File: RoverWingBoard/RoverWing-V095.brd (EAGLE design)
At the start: 81.3 x 81.3 mm, 80 parts, among them J1 HEADER-VH, J10 HEADER-PH-4P, J11 HEADER-PH-3P, J12 HEADER-3X04, J13 HEADER-3X06", J14 HEADER-2X16, J15 HEADER-2X12, J16 DF13-4P-1.25DSA, J17 DF13-6P-1.25DSA, J2 HEADER-VH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

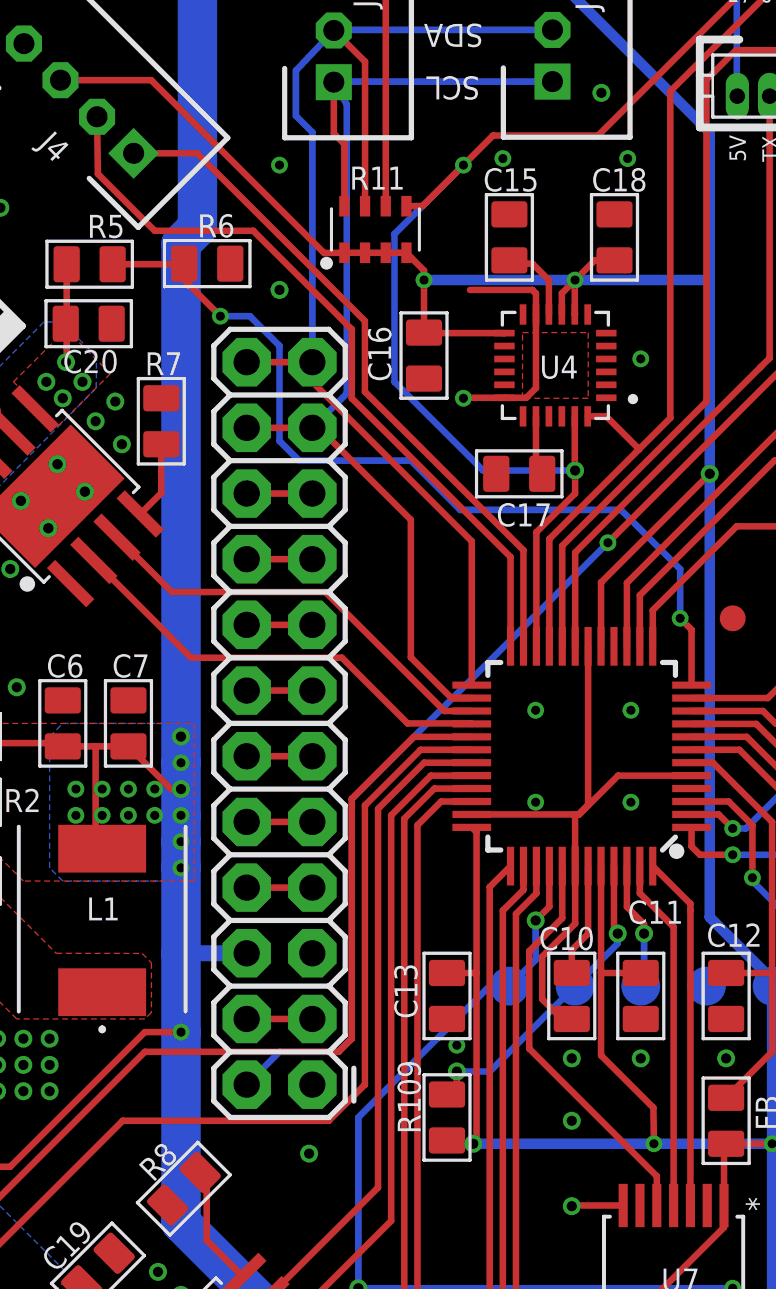
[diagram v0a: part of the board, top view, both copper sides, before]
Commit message: V095 - fixed NeoPixel signals and added the covers
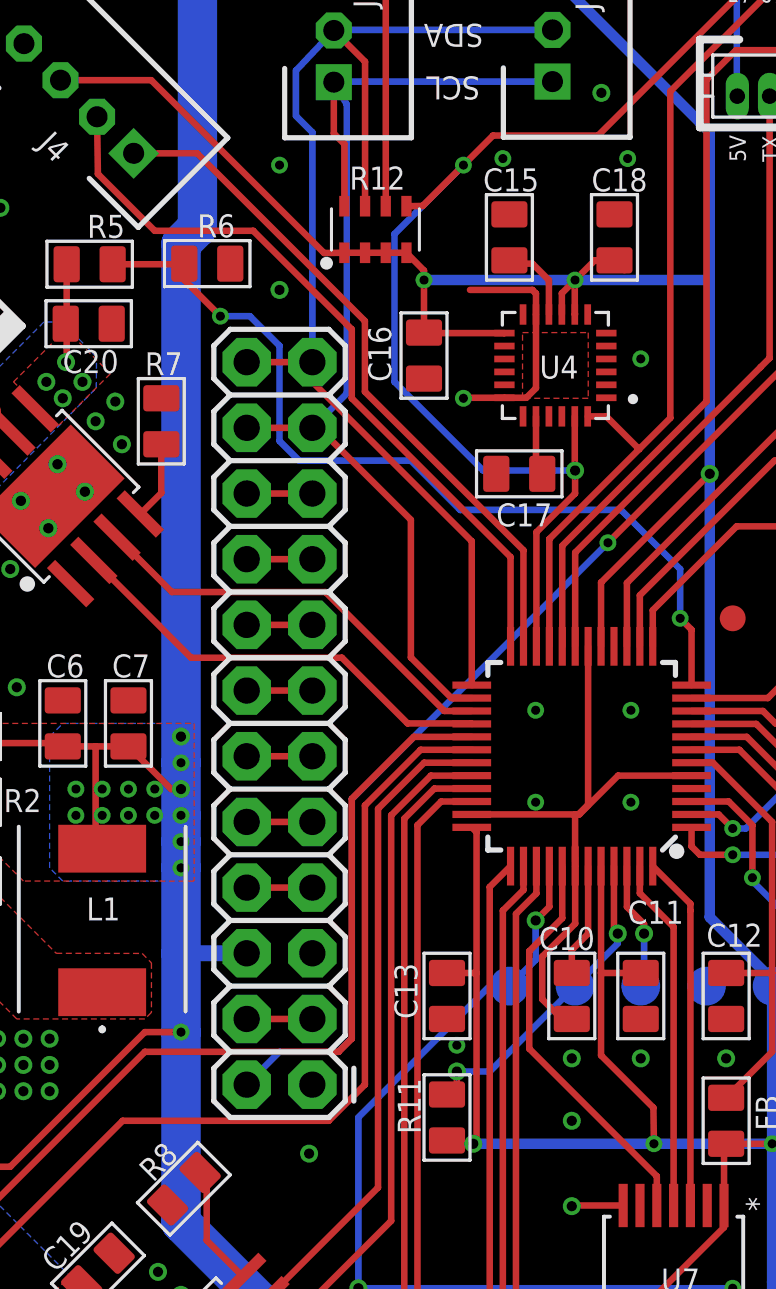
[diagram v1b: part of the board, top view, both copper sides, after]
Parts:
- removed R109: 1k, RoverWing:0805
- added R12: 2.7k*4, RoverWing:0603*4
- R11: value 2.7k*4 -> 1k; device RoverWing:0603*4 -> RoverWing:0805
- moved R11 34.5 mm to (-4.95, -10.2)
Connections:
- net 3.3V: now also R12.1, R12.2, R12.3, R12.4; no longer R109.1, R11.2, R11.3, R11.4
- net SCL1: now also R12.8; no longer R11.8
- net SCL2: now also R12.5; no longer R11.5
- net SDA1: now also R12.7; no longer R11.7
- net SDA2: now also R12.6; no longer R11.6
- net SWCLK: now also R11.2; no longer R109.2
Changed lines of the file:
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@@
 <attribute name="VALUE" x="-34.667" y="4.386" size="1.27" layer="27"/>
 </element>
-<element name="R109" library="RoverWing" package="0805" value="1k" x="-4.953" y="-10.16" smashed="yes" rot="R90">
+<element name="R11" library="RoverWing" package="0805" value="1k" x="-4.953" y="-10.16" smashed="yes" rot="R90">
 <attribute name="NAME" x="-5.969" y="-10.795" size="0.889" layer="25" font="vector" ratio="11" rot="R90"/>
 <attribute name="VALUE" x="-6.858" y="-12.319" size="0.635" layer="27" ratio="10"/>
 </element>
-<element name="R11" library="RoverWing" package="0603*4" value="2.7k*4" x="-7.7216" y="24.1808" smashed="yes" rot="R90">
+<element name="R12" library="RoverWing" package="0603*4" value="2.7k*4" x="-7.7216" y="24.1808" smashed="yes" rot="R90">
 <attribute name="NAME" x="-7.6454" y="26.6129" size="0.889" layer="25" font="vector" ratio="11" rot="R180" align="bottom-center"/>
 <attribute name="PARTNO" value="RTA03-4D272JTP " x="-7.7216" y="24.1808" size="1.778" layer="27" rot="R90" display="off"/>
@@
 <via x="7.62" y="-11.176" extent="1-16" drill="0.35"/>
 <wire x1="5.842" y1="-11.176" x2="7.62" y2="-11.176" width="0.254" layer="1"/>
-<contactref element="R109" pad="1"/>
 <contactref element="R11" pad="1"/>
-<contactref element="R11" pad="2"/>
-<contactref element="R11" pad="3"/>
-<contactref element="R11" pad="4"/>
+<contactref element="R12" pad="1"/>
+<contactref element="R12" pad="2"/>
+<contactref element="R12" pad="3"/>
+<contactref element="R12" pad="4"/>
 <wire x1="-5.842" y1="22.225" x2="-5.842" y2="22.5912" width="0.254" layer="1"/>
 <wire x1="-5.842" y1="22.5912" x2="-6.5216" y2="23.2808" width="0.254" layer="1"/>
@@
 <contactref element="U1" pad="45"/>
 <via x="-4.572" y="-8.382" extent="1-16" drill="0.3937"/>
-<contactref element="R109" pad="2"/>
+<contactref element="R11" pad="2"/>
 <wire x1="-4.572" y1="-8.382" x2="-4.572" y2="-8.89" width="0.254" layer="1"/>
 <wire x1="-4.953" y1="-9.271" x2="-4.572" y2="-8.89" width="0.254" layer="1"/>
@@
 <wire x1="-9.329984375" y1="29.877590625" x2="-8.831015625" y2="29.019409375" width="0.254" layer="16"/>
 <wire x1="-10.16" y1="16.51" x2="-12.7" y2="16.51" width="0.254" layer="1"/>
-<contactref element="R11" pad="8"/>
+<contactref element="R12" pad="8"/>
 <wire x1="-3.996" y1="6.06" x2="-4.78113125" y2="6.06" width="0.254" layer="1"/>
 <wire x1="-4.78113125" y1="6.06" x2="-6.35" y2="7.62886875" width="0.254" layer="1"/>
@@
 <wire x1="-3.996" y1="12.124" x2="-10.16" y2="18.288" width="0.254" layer="1"/>
 <wire x1="-10.16" y1="19.05" x2="-12.7" y2="19.05" width="0.254" layer="1"/>
-<contactref element="R11" pad="7"/>
+<contactref element="R12" pad="7"/>
 <wire x1="-3.996" y1="12.124" x2="-3.996" y2="6.56" width="0.254" layer="1"/>
 <wire x1="-8.1216" y1="25.0808" x2="-8.1216" y2="30.66920625" width="0.254" layer="1"/>
@@
 <wire x1="3.683" y1="29.5242625" x2="8.753" y2="34.5942625" width="0.254" layer="1"/>
 <wire x1="3.683" y1="29.5242625" x2="3.683" y2="16.891" width="0.254" layer="1"/>
-<contactref element="R11" pad="6"/>
+<contactref element="R12" pad="6"/>
 <wire x1="-0.996" y1="12.212" x2="-0.996" y2="8.06" width="0.254" layer="1"/>
 <wire x1="-7.3216" y1="25.0808" x2="-7.3216" y2="35.4774" width="0.254" layer="1"/>
@@
 <wire x1="-4.318" y1="26.67" x2="-3.175" y2="27.813" width="0.254" layer="1"/>
 <wire x1="-4.318" y1="26.67" x2="-6.985" y2="24.003" width="0.254" layer="16"/>
-<contactref element="R11" pad="5"/>
+<contactref element="R12" pad="5"/>
 <wire x1="-1.496" y1="12.474" x2="-1.496" y2="8.06" width="0.254" layer="1"/>
 <wire x1="-6.5216" y1="25.0808" x2="-5.8972" y2="25.0908" width="0.254" layer="1"/>
